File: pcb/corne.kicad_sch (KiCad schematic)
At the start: 146 parts, among them J1 MJ-4PP-9, J2 OLED, J3 MJ-4PP-9, J4 OLED, SW1 SW_PUSH, SW10 SW_PUSH, SW11 SW_PUSH, SW12 SW_PUSH, SW13 SW_PUSH, SW14 SW_PUSH, SW15 SW_PUSH, SW16 SW_PUSH, SW17 SW_PUSH, SW18 SW_PUSH, SW19 SW_PUSH, SW2 SW_PUSH, SW20 SW_PUSH, SW21 SW_PUSH, SW22 SW_PUSH, SW23 SW_PUSH, SW24 SW_PUSH, SW25 SW_PUSH, SW26 SW_PUSH, SW27 SW_PUSH, SW28 SW_PUSH, SW29 SW_PUSH, SW3 SW_PUSH, SW30 SW_PUSH, SW31 SW_PUSH, SW32 SW_PUSH, SW33 SW_PUSH, SW34 SW_PUSH, SW35 SW_PUSH, SW36 SW_PUSH, SW37 SW_PUSH, SW38 SW_PUSH, SW39 SW_PUSH, SW4 SW_PUSH, SW40 SW_PUSH, SW41 SW_PUSH, SW42 SW_PUSH, SW5 SW_PUSH, SW6 SW_PUSH, SW7 SW_PUSH, SW8 SW_PUSH, SW9 SW_PUSH, U1 ProMicro, U2 ProMicro

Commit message: Update sch
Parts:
- removed D22, D25, D26, D27, D28, D29, D30, D31, D32, D33, D34, D35, D36, D37, D38, D39, D40, D41, D42: D, kbd:D3_SMD_v2, symbol Device:D
- removed J1, J3: MJ-4PP-9, kbd:MJ-4PP-9_1side, symbol kbd:MJ-4PP-9
- removed J4: OLED, kbd:OLED_1side, symbol Connector_Generic:Conn_01x04
- removed LED1, LED2, LED28, LED29, LED3, LED30, LED31, LED32, LED33, LED4, LED5, LED6: WS2812B, LED_SMD:LED_WS2812B_PLCC4_5.0x5.0mm_P3.2mm, symbol LED:WS2812B
- removed LED34, LED35, LED36, LED37, LED38, LED39, LED40, LED41, LED42, LED43, LED44, LED45, LED46, LED47, LED48, LED49, LED50, LED51, LED52, LED53, LED54: YS-SK6812MINI-E, kbd:YS-SK6812MINI-E, symbol kbd:YS-SK6812MINI-E
- removed RSW1, RSW2: SW_PUSH, kbd:ResetSW_1side, symbol kbd:SW_PUSH
- removed SW1, SW10, SW11, SW12, SW13, SW14, SW15, SW16, SW17, SW18, SW19, SW2, SW20, SW22, SW23, SW24, SW25, SW26, SW27, SW28, SW29, SW3, SW30, SW31, SW32, SW33, SW34, SW35, SW36, SW37, SW38, SW39, SW4, SW40, SW41, SW5, SW6, SW7, SW8, SW9: SW_PUSH, kbd:CherryMX_Hotswap, symbol kbd:SW_PUSH
- removed SW21, SW42: SW_PUSH, kbd:CherryMX_Hotswap_1.5u, symbol kbd:SW_PUSH
- removed U1, U2: ProMicro, kbd:ProMicro_v3, symbol kbd:ProMicro
- added C1, C2: 20p, symbol Device:C_Small
- added C10, C12, C13, C14, C15, C3, C4, C7, C9: 100n, symbol Device:C_Small
- added C11, C6: 10u, symbol Device:C_Small
- added C16, C5, C8: 1u, symbol Device:C_Small
- added D1: ESD5Z5V0, Diode_SMD:D_SOD-523, symbol Diode:ESD5Zxx
- added F1: SMD0805-050-16V, symbol Device:Fuse
- added J1: TYPE-C-31-M-13C, symbol Connector:USB_C_Receptacle_USB2.0
- added J2: ST-0277D00-052-142, symbol Connector_Audio:AudioJack4
- added J4: Conn_01x03, symbol Connector_Generic:Conn_01x03
- added J5, J6: Conn_01x06, symbol Connector_Generic:Conn_01x06
- added LED22, LED23: YS-SK6812MINI-E, kbd:YS-SK6812MINI-E, symbol kbd_local:YS-SK6812MINI-E
- added R1, R2: 5.1k, symbol Device:R_Small
- added R3, R6: 1k, symbol Device:R
- added R4, R5: 27, symbol Device:R_Small
- added R7: 10k, symbol Device:R
- added SMDSW1, SMDSW2: SKQGADE010, Button_Switch_SMD:SW_SPST_SKQG_WithStem, symbol Switch:SW_Push
- added SW1, SW10, SW11, SW12, SW13, SW14, SW15, SW16, SW17, SW18, SW19, SW2, SW20, SW21, SW3, SW4, SW5, SW6, SW7, SW8, SW9: SW_Push, kbd:keyswitch_cherrymx_hotswap_1u, symbol Switch:SW_Push
- added SW22, SW23: RotaryEncoder_Switch, symbol Device:RotaryEncoder_Switch
- added U1: RP2040, Package_DFN_QFN:QFN-56-1EP_7x7mm_P0.4mm_EP3.2x3.2mm, symbol MCU_RaspberryPi:RP2040
- added U2: NCP1117LPST33T3G, Package_TO_SOT_SMD:SOT-223-3_TabPin2, symbol Regulator_Linear:NCP1117-3.3_SOT223
- added U3: TPD4E05U06DQAR, Package_SON:USON-10_2.5x1.0mm_P0.5mm, symbol Power_Protection:TPD4EUSB30
- added U4: W25Q128JVSIQ, Package_SON:WSON-8-1EP_6x5mm_P1.27mm_EP3.4x4.3mm, symbol Memory_Flash:W25Q128JVS
- added Y1: 12MHz 10pF, Crystal:Crystal_SMD_2520-4Pin_2.5x2.0mm, symbol Device:Crystal_GND24_Small
- J3: renamed from J2; value OLED -> Conn_01x04
- LED1: renamed from LED7; symbol kbd:YS-SK6812MINI-E -> kbd_local:YS-SK6812MINI-E
- LED10: symbol kbd:YS-SK6812MINI-E -> kbd_local:YS-SK6812MINI-E
- LED11: renamed from LED16; symbol kbd:YS-SK6812MINI-E -> kbd_local:YS-SK6812MINI-E
- LED12: renamed from LED22; symbol kbd:YS-SK6812MINI-E -> kbd_local:YS-SK6812MINI-E
- LED13: renamed from LED25; symbol kbd:YS-SK6812MINI-E -> kbd_local:YS-SK6812MINI-E
- LED14: renamed from LED11; symbol kbd:YS-SK6812MINI-E -> kbd_local:YS-SK6812MINI-E
- LED15: renamed from LED17; symbol kbd:YS-SK6812MINI-E -> kbd_local:YS-SK6812MINI-E
- LED16: renamed from LED23; symbol kbd:YS-SK6812MINI-E -> kbd_local:YS-SK6812MINI-E
- LED17: renamed from LED26; symbol kbd:YS-SK6812MINI-E -> kbd_local:YS-SK6812MINI-E
- LED18: renamed from LED12; symbol kbd:YS-SK6812MINI-E -> kbd_local:YS-SK6812MINI-E
- LED19: renamed from LED18; symbol kbd:YS-SK6812MINI-E -> kbd_local:YS-SK6812MINI-E
- LED2: renamed from LED13; symbol kbd:YS-SK6812MINI-E -> kbd_local:YS-SK6812MINI-E
- LED20: renamed from LED24; symbol kbd:YS-SK6812MINI-E -> kbd_local:YS-SK6812MINI-E
- LED21: renamed from LED27; symbol kbd:YS-SK6812MINI-E -> kbd_local:YS-SK6812MINI-E
- LED3: renamed from LED19; symbol kbd:YS-SK6812MINI-E -> kbd_local:YS-SK6812MINI-E
- LED4: renamed from LED8; symbol kbd:YS-SK6812MINI-E -> kbd_local:YS-SK6812MINI-E
- LED5: renamed from LED14; symbol kbd:YS-SK6812MINI-E -> kbd_local:YS-SK6812MINI-E
- LED6: renamed from LED20; symbol kbd:YS-SK6812MINI-E -> kbd_local:YS-SK6812MINI-E
- LED7: renamed from LED9; symbol kbd:YS-SK6812MINI-E -> kbd_local:YS-SK6812MINI-E
- LED8: renamed from LED15; symbol kbd:YS-SK6812MINI-E -> kbd_local:YS-SK6812MINI-E
- LED9: renamed from LED21; symbol kbd:YS-SK6812MINI-E -> kbd_local:YS-SK6812MINI-E
- renumbered D15 to D10, D4 to D11, D10 to D12, D16 to D13, D19 to D14, D5 to D15, D11 to D16, D20 to D18, D6 to D19, D1 to D2, D12 to D20, D18 to D21, D21 to D22, D7 to D3, D13 to D4, D2 to D5, D8 to D6, D14 to D7, D3 to D8
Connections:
- net row1 is gone; now on net ROW1: D12.1 (K), D16.1 (K), D20.1 (K), D3.1 (K), D6.1 (K), D9.1 (K)
- net GND: now also C1.2, C10.2, C11.2, C12.2, C13.2, C14.2, C15.2, C16.2, C2.2, C3.2, C4.2, C5.2, C6.2, C7.2, C8.2, C9.2, D1.2 (A), J1.A1 (GND), J1.A12 (GND), J1.B1 (GND), J1.B12 (GND), J1.S1 (SHIELD), J2.S, J4.2 (Pin_2), J5.1 (Pin_1), J6.1 (Pin_1), LED22.3 (VSS), LED23.3 (VSS), R1.1, R2.1, SMDSW1.1, SMDSW2.1, SW22.C, SW23.C, U1.19 (TESTEN), U1.57 (GND), U2.1 (GND), U3.3 (GND), U3.8 (GND), U4.4 (GND), Y1.2, Y1.4
- net LED: now also LED22.4 (DIN), U1.31 (GPIO20)
- net SCL: now also U1.5 (GPIO3)
- net SDA: now also U1.4 (GPIO2)
- net at D5.2 (A): now also SW4.2
- net at D8.2 (A): now also SW7.2
- net at D11.2 (A): now also SW10.2
- net at D15.2 (A): now also SW14.2
- net at D19.2 (A): now also SW18.2
- net at D2.2 (A): now also SW1.2
- net at D6.2 (A): now also SW5.2
- net at D9.2 (A): now also SW8.2
- net at D12.2 (A): now also SW11.2
- net at D16.2 (A): now also SW15.2
- net at D20.2 (A): now also SW19.2
- net at D3.2 (A): now also SW2.2
- net at D7.2 (A): now also SW6.2
- net at D10.2 (A): now also SW9.2
- net at D13.2 (A): now also SW12.2
- net at D17.2 (A): now also SW16.2
- net at D21.2 (A): now also SW20.2
- net at D4.2 (A): now also SW3.2
- net at D18.2 (A): now also SW17.2
- net at D22.2 (A): now also SW21.2
- net at D14.2 (A): now also SW13.2
- net at D23.2 (A): now also SW22.S1
- net at D24.2 (A): now also SW23.S1
- net at LED21.4 (DIN): now also LED23.2 (DOUT)
- net VCC renamed +5V
- net +5V: now also C6.1, F1.2, J2.T, J5.6 (Pin_6), J6.6 (Pin_6), LED22.1 (VDD), LED23.1 (VDD), U2.3 (VI)
- net row0 renamed ROW0
- net ROW0: now also D23.1 (K), U1.14 (GPIO11)
- net row0_r renamed ROW1
- net ROW1: now also U1.15 (GPIO12); no longer D23.1 (K)
- net row2 renamed ROW2
- net ROW2: now also U1.16 (GPIO13)
- net row3 renamed ROW3
- net ROW3: now also U1.17 (GPIO14)
- new net: C1.1, U1.20 (XIN), Y1.1
- new net: C2.1, R3.1, Y1.3
- new net: R5.1, U1.46 (USB_DM)
- new net: R3.2, U1.21 (XOUT)
- new net: SMDSW2.2, U1.26 (RUN)
- new net: R4.2, U1.47 (USB_DP)
- new net: LED22.2 (DOUT), LED23.4 (DIN)
- new net: J1.A5 (CC1), R1.2
- new net: J1.B5 (CC2), R2.2
- new net: R6.2, SMDSW1.2
- new net +1V1: C3.1, C4.1, C5.1, U1.23 (DVDD), U1.45 (VREG_VOUT), U1.50 (DVDD)
- new net +3V3: C10.1, C11.1, C12.1, C13.1, C14.1, C15.1, C16.1, C7.1, C8.1, C9.1, R7.2, U1.1 (IOVDD), U1.10 (IOVDD), U1.22 (IOVDD), U1.32 (GPIO21), U1.33 (IOVDD), U1.42 (IOVDD), U1.43 (ADC_AVDD), U1.44 (VREG_IN), U1.48 (USB_VDD), U1.49 (IOVDD), U2.2 (VO), U4.8 (VCC)
- new net COL0: SW1.1, SW2.1, SW3.1, U1.6 (GPIO4)
- new net COL1: SW4.1, SW5.1, SW6.1, U1.7 (GPIO5)
- new net COL2: SW7.1, SW8.1, SW9.1, U1.8 (GPIO6)
- new net COL3: SW10.1, SW11.1, SW12.1, SW13.1, U1.9 (GPIO7)
- new net COL4: SW14.1, SW15.1, SW16.1, SW17.1, U1.11 (GPIO8)
- new net COL5: SW18.1, SW19.1, SW20.1, SW21.1, U1.12 (GPIO9)
- new net COL6: SW22.S2, SW23.S2, U1.13 (GPIO10)
- new net D+: J1.A6 (D+), J1.B6 (D+), R4.1, U3.4 (D2+), U3.5 (D2-), U3.6 (NC), U3.7 (NC)
- new net D-: J1.A7 (D-), J1.B7 (D-), R5.2, U3.1 (D1+), U3.10 (NC), U3.2 (D1-), U3.9 (NC)
- new net GPIO22: J5.5 (Pin_5), U1.34 (GPIO22)
- new net GPIO23: J5.4 (Pin_4), U1.35 (GPIO23)
- new net GPIO24: J5.3 (Pin_3), U1.36 (GPIO24)
- new net GPIO25: J5.2 (Pin_2), U1.37 (GPIO25)
- new net GPIO26: J6.5 (Pin_5), U1.38 (GPIO26_ADC0)
- new net GPIO27: J6.4 (Pin_4), U1.39 (GPIO27_ADC1)
- new net GPIO28: J6.3 (Pin_3), U1.40 (GPIO28_ADC2)
- new net GPIO29: J6.2 (Pin_2), U1.41 (GPIO29_ADC3)
- new net QSPI_SCLK: U1.52 (QSPI_SCLK), U4.6 (CLK)
- new net QSPI_SD0: U1.53 (QSPI_SD0), U4.5 (DI(IO0))
- new net QSPI_SD1: U1.55 (QSPI_SD1), U4.2 (DO(IO1))
- new net QSPI_SD2: U1.54 (QSPI_SD2), U4.3 (IO2)
- new net QSPI_SD3: U1.51 (QSPI_SD3), U4.7 (IO3)
- new net QSPI_SS: R6.1, R7.1, U1.56 (QSPI_SS), U4.1 (~{CS})
- new net RE0A: SW22.A, U1.27 (GPIO16)
- new net RE0B: SW22.B, U1.28 (GPIO17)
- new net RE1A: SW23.A, U1.29 (GPIO18)
- new net RE1B: SW23.B, U1.30 (GPIO19)
- new net RX: J2.R1, U1.3 (GPIO1)
- new net SWCLK: J4.1 (Pin_1), U1.24 (SWCLK)
- new net SWD: J4.3 (Pin_3), U1.25 (SWD)
- new net TX: J2.R2, U1.2 (GPIO0)
- new net VBUS: D1.1 (K), F1.1, J1.A4 (VBUS), J1.A9 (VBUS), J1.B4 (VBUS), J1.B9 (VBUS)
- no-connect marks 14 -> 4
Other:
- note added: "DEBUG"
- note added: "Extention"
- note added: "Flash memory"
- note added: "Key switches"
- note added: "LDO"
- note added: "LEDs"
- note added: "MCU RP2040"
- note added: "OLED"
- note added: "POWER"
- note added: "RP2040 original pins"
- note added: "SPLIT_HAND_PIN"
- note added: "T(4,5), R1(3), R2(2), S(1)"
- note added: "TRRS"
- note added: "USB ESD"
- note added: "VBUS USD"
- note added: "boot switch"
- note added: "close to pin 44"
- note added: "close to pin 45"
- note added: "left R1:RX, R2:TX right R1:TX, R2:RX"
- title: Corne Cherry -> Corne
- moved on the sheet: D10, D11, D12, D13, D14, D15, D16, D17, D18, D19, D2, D20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

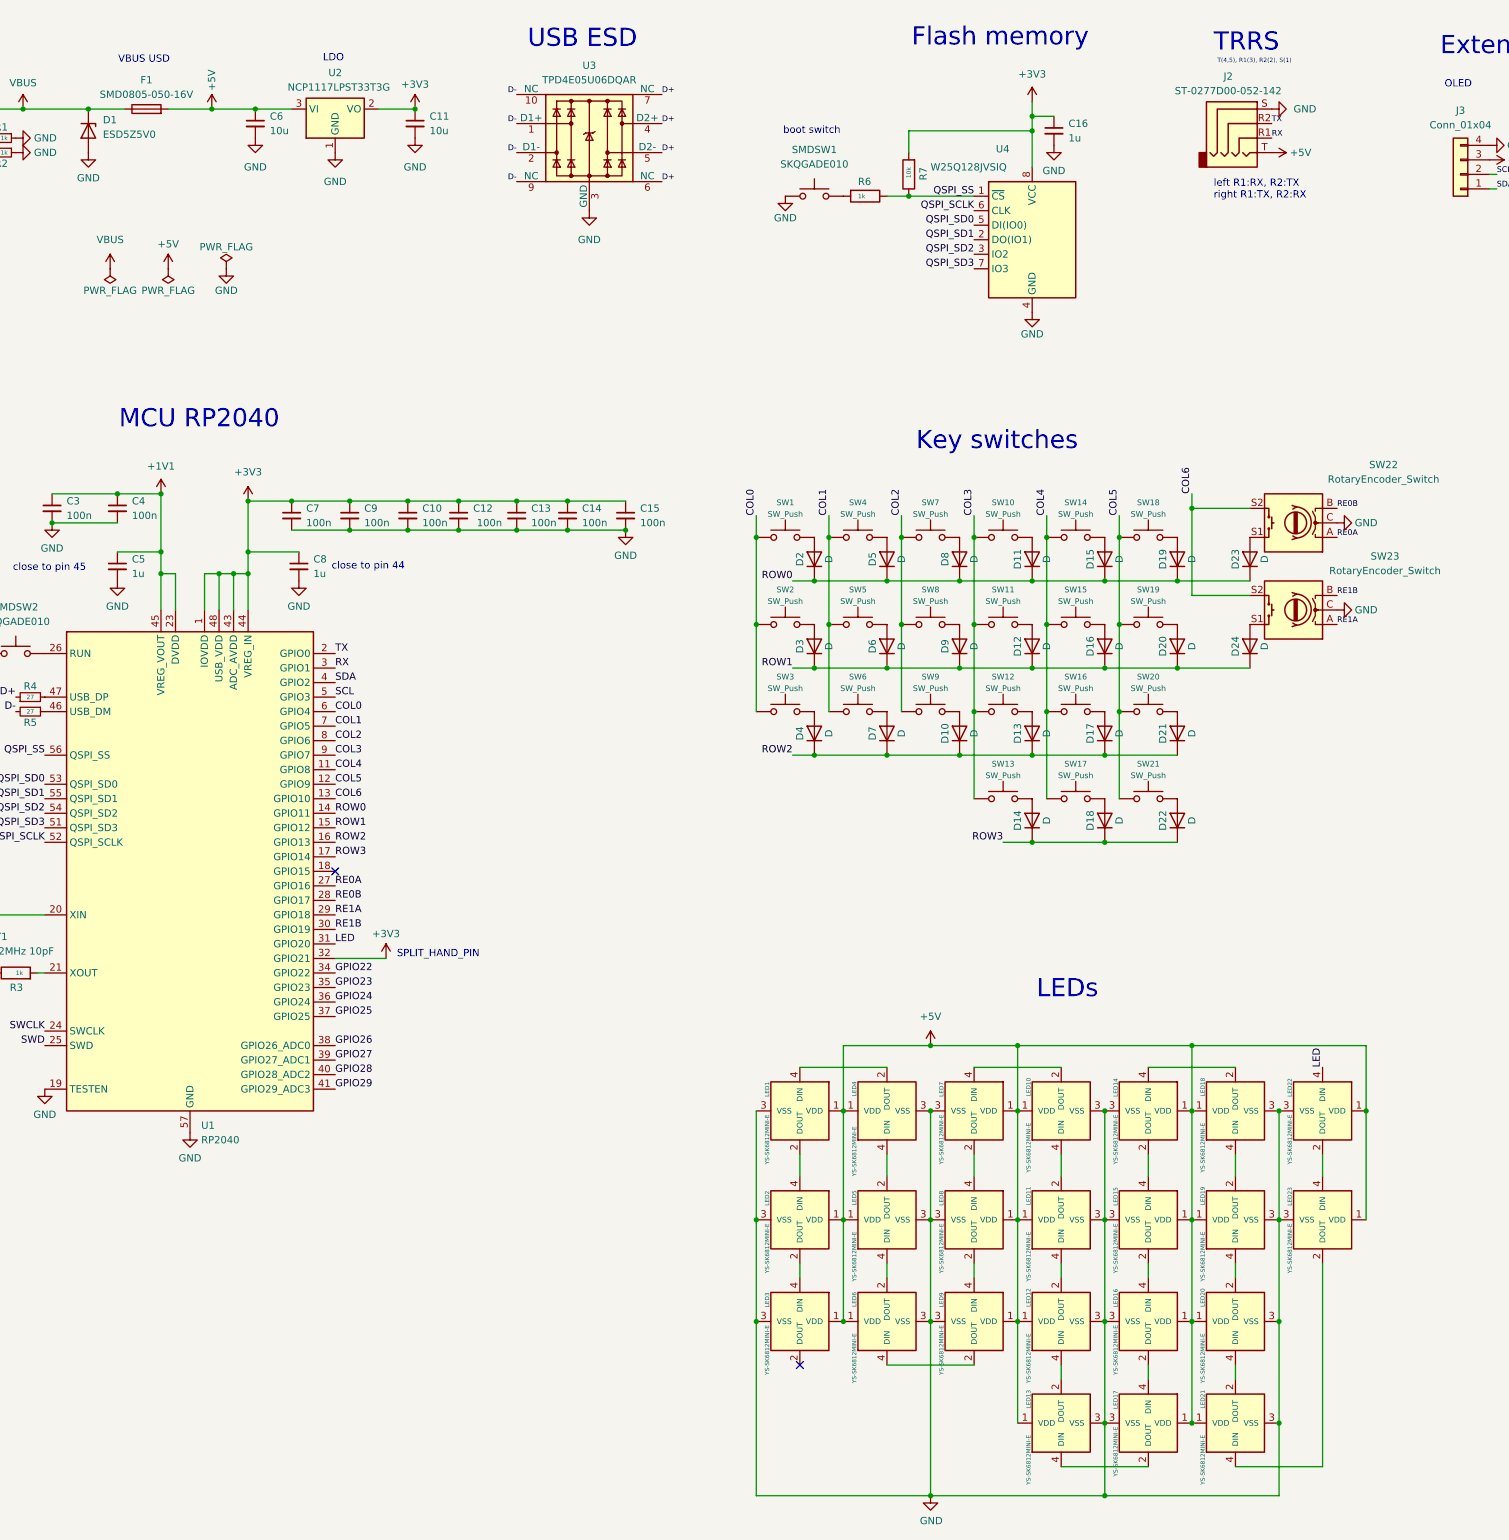
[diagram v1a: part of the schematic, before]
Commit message: Add assigns
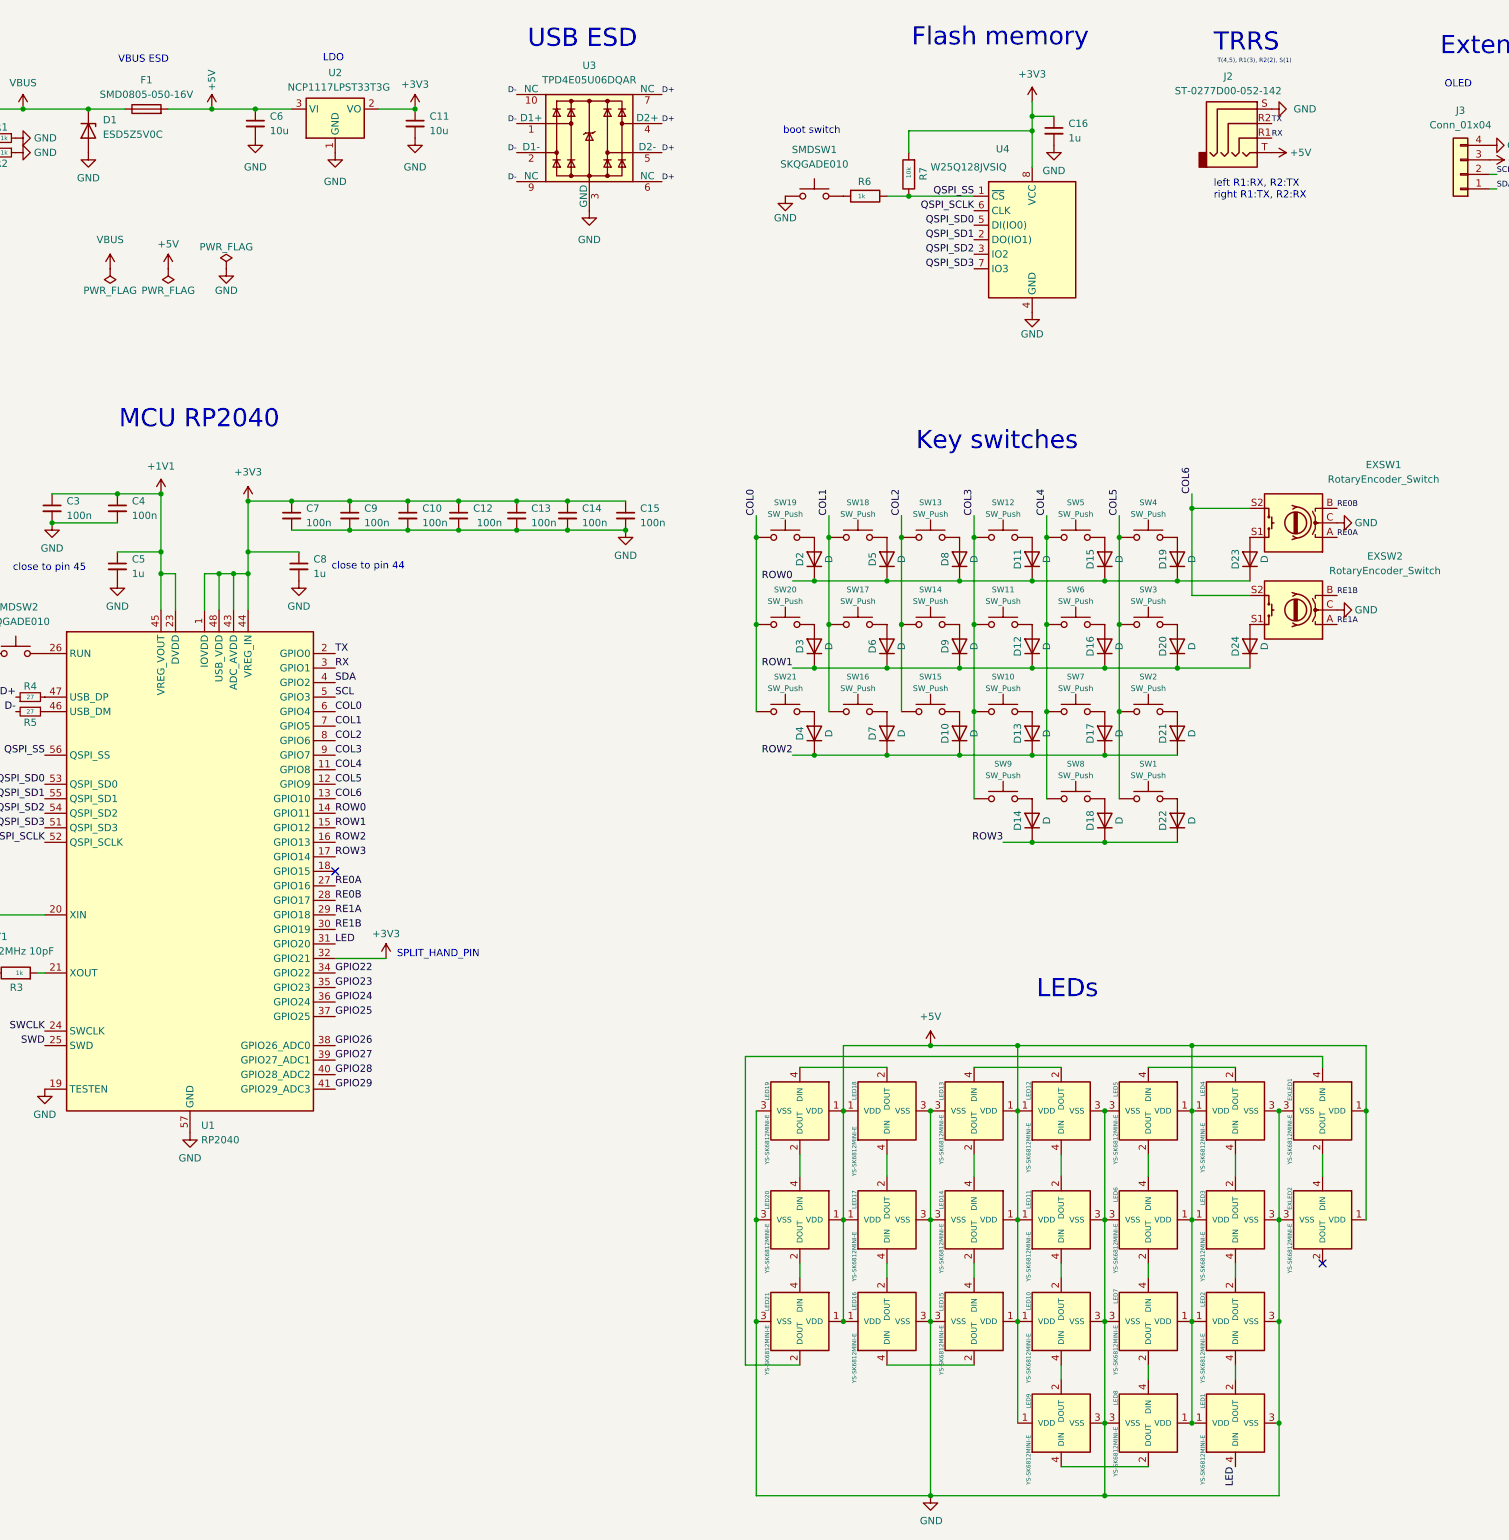
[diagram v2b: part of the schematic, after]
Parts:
- D1: value ESD5Z5V0 -> ESD5Z5V0C; JLCPCB Part # (none) -> C2901325
- EXSW1: renamed from SW22; footprint (none) -> kbd_local:keyswitch_cherrymx_hotswap_1u_rotary_encoder_ec12
- EXSW2: renamed from SW23; footprint (none) -> kbd_local:keyswitch_cherrymx_hotswap_1u_rotary_encoder_ec12
- F1: footprint (none) -> Fuse:Fuse_0805_2012Metric; JLCPCB Part # (none) -> C2833485
- renumbered LED22 to EXLED1, LED23 to EXLED2, LED21 to LED1, LED12 to LED10, LED10 to LED12, LED7 to LED13, LED8 to LED14, LED9 to LED15, LED6 to LED16, LED5 to LED17, LED4 to LED18, LED1 to LED19, LED20 to LED2, LED2 to LED20, LED3 to LED21, LED19 to LED3, LED18 to LED4, LED14 to LED5, LED15 to LED6, LED16 to LED7, LED17 to LED8, LED13 to LED9, SW21 to SW1, SW12 to SW10, SW10 to SW12, SW7 to SW13, SW8 to SW14, SW9 to SW15, SW6 to SW16, SW5 to SW17, SW4 to SW18, SW1 to SW19, SW20 to SW2, SW2 to SW20, SW3 to SW21, SW19 to SW3, SW18 to SW4, SW14 to SW5, SW15 to SW6, SW16 to SW7, SW17 to SW8, SW13 to SW9
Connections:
- net LED: now also LED1.4 (DIN); no longer EXLED1.4 (DIN)
- net at LED21.2 (DOUT): now also EXLED1.4 (DIN)
- net at EXLED2.2 (DOUT): no longer LED1.4 (DIN)
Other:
- note added: "VBUS ESD"
- note removed: "VBUS USD"

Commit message: Update pcb
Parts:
- C1, C10, C11, C12, C13, C14, C15, C16, C2, C3, C4, C5, C6, C7, C8, C9: footprint (none) -> Capacitor_SMD:C_0603_1608Metric
- D1: renamed from D22; footprint kbd:D3_SMD_v2 -> Diode_SMD:D_0603_1608Metric
- D10: renamed from D13; footprint kbd:D3_SMD_v2 -> Diode_SMD:D_0603_1608Metric
- D11: renamed from D12; footprint kbd:D3_SMD_v2 -> Diode_SMD:D_0603_1608Metric
- D12: renamed from D11; footprint kbd:D3_SMD_v2 -> Diode_SMD:D_0603_1608Metric
- D13: renamed from D8; footprint kbd:D3_SMD_v2 -> Diode_SMD:D_0603_1608Metric
- D14: renamed from D9; footprint kbd:D3_SMD_v2 -> Diode_SMD:D_0603_1608Metric
- D15: renamed from D10; footprint kbd:D3_SMD_v2 -> Diode_SMD:D_0603_1608Metric
- D16: renamed from D7; footprint kbd:D3_SMD_v2 -> Diode_SMD:D_0603_1608Metric
- D17: renamed from D6; footprint kbd:D3_SMD_v2 -> Diode_SMD:D_0603_1608Metric
- D18: renamed from D5; footprint kbd:D3_SMD_v2 -> Diode_SMD:D_0603_1608Metric
- D19: renamed from D2; footprint kbd:D3_SMD_v2 -> Diode_SMD:D_0603_1608Metric
- D2: renamed from D21; footprint kbd:D3_SMD_v2 -> Diode_SMD:D_0603_1608Metric
- D20: renamed from D3; footprint kbd:D3_SMD_v2 -> Diode_SMD:D_0603_1608Metric
- D21: renamed from D4; footprint kbd:D3_SMD_v2 -> Diode_SMD:D_0603_1608Metric
- D3: renamed from D20; footprint kbd:D3_SMD_v2 -> Diode_SMD:D_0603_1608Metric
- D4: renamed from D19; footprint kbd:D3_SMD_v2 -> Diode_SMD:D_0603_1608Metric
- D5: renamed from D15; footprint kbd:D3_SMD_v2 -> Diode_SMD:D_0603_1608Metric
- D6: renamed from D16; footprint kbd:D3_SMD_v2 -> Diode_SMD:D_0603_1608Metric
- D7: renamed from D17; footprint kbd:D3_SMD_v2 -> Diode_SMD:D_0603_1608Metric
- D8: renamed from D18; footprint kbd:D3_SMD_v2 -> Diode_SMD:D_0603_1608Metric
- D9: renamed from D14; footprint kbd:D3_SMD_v2 -> Diode_SMD:D_0603_1608Metric
- EXD1: renamed from D23; footprint kbd:D3_SMD_v2 -> Diode_SMD:D_0603_1608Metric
- EXD2: renamed from D24; footprint kbd:D3_SMD_v2 -> Diode_SMD:D_0603_1608Metric
- EXLED1, EXLED2, LED1, LED10, LED11, LED12, LED13, LED14, LED15, LED16, LED17, LED18, LED19, LED2, LED20, LED21, LED3, LED4, LED5, LED6, LED7, LED8, LED9: footprint kbd:YS-SK6812MINI-E -> kbd_local:YS-SK6812MINI-E
- F1: value SMD0805-050-16V -> BSMD0603-050-12V; footprint Fuse:Fuse_0805_2012Metric -> Fuse:Fuse_0603_1608Metric; JLCPCB Part # C2833485 -> C2844464
- J1: footprint (none) -> kbd_local:TYPE-C-31-M-13C
- J2: footprint (none) -> kbd_local:ST-0277D00-052-142
- J3: footprint kbd:OLED_1side -> kbd_local:OLED
- J4: footprint (none) -> Connector_PinHeader_2.54mm:PinHeader_1x03_P2.54mm_Vertical
- J5, J6: footprint (none) -> Connector_PinHeader_2.54mm:PinHeader_1x06_P2.54mm_Vertical
- R1, R2, R3, R4, R5, R6, R7: footprint (none) -> Resistor_SMD:R_0603_1608Metric
- renumbered D1 to ZD1
